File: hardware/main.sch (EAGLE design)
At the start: 16 parts, among them IC1 ATMEGA168-AU, J1 AVR_SPI_PRG_6NS

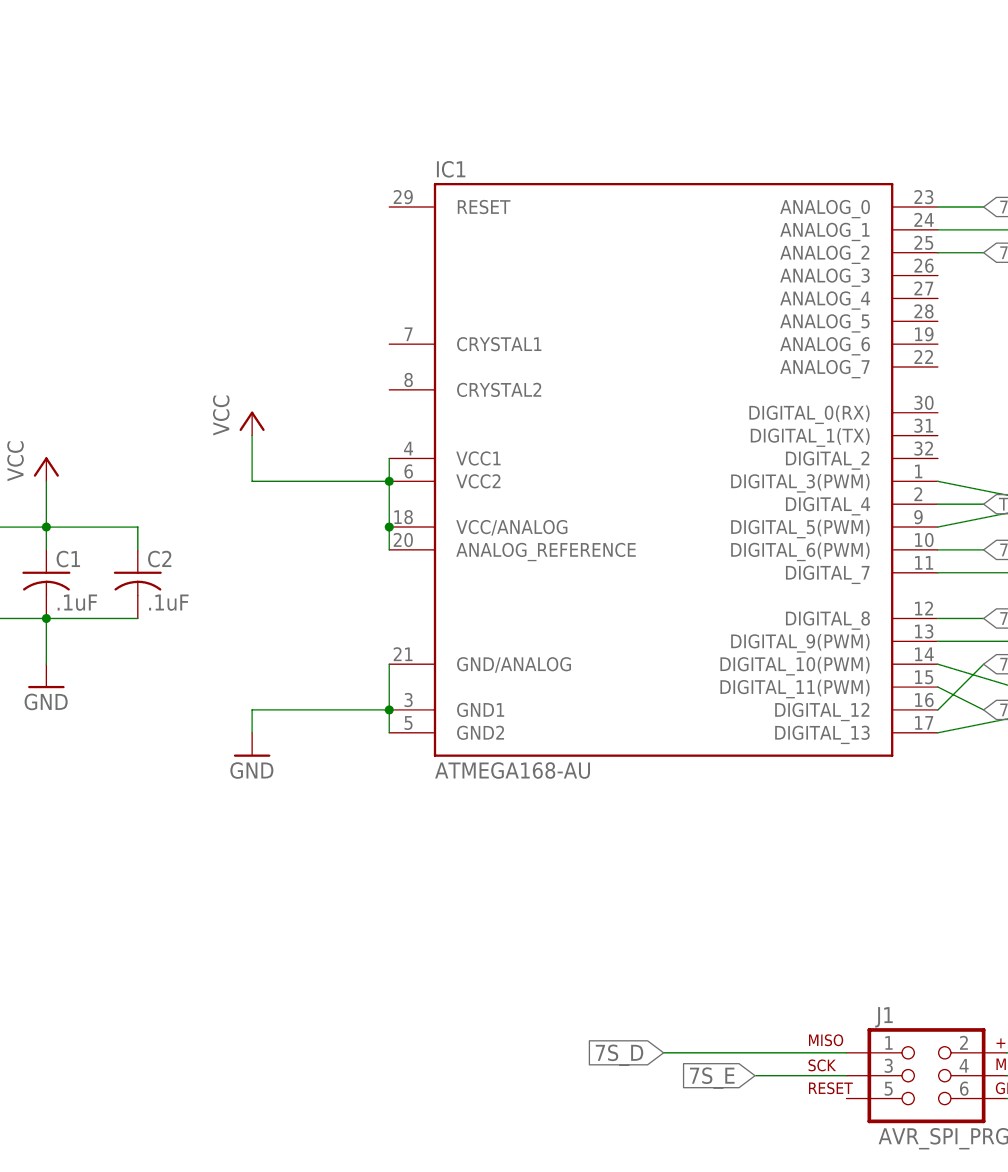
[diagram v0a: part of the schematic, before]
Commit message: HARDWARE MISTAKE: Did not include connection to Reset line. This makes the AVR unprogrammable without a jumper wire. Fixed.
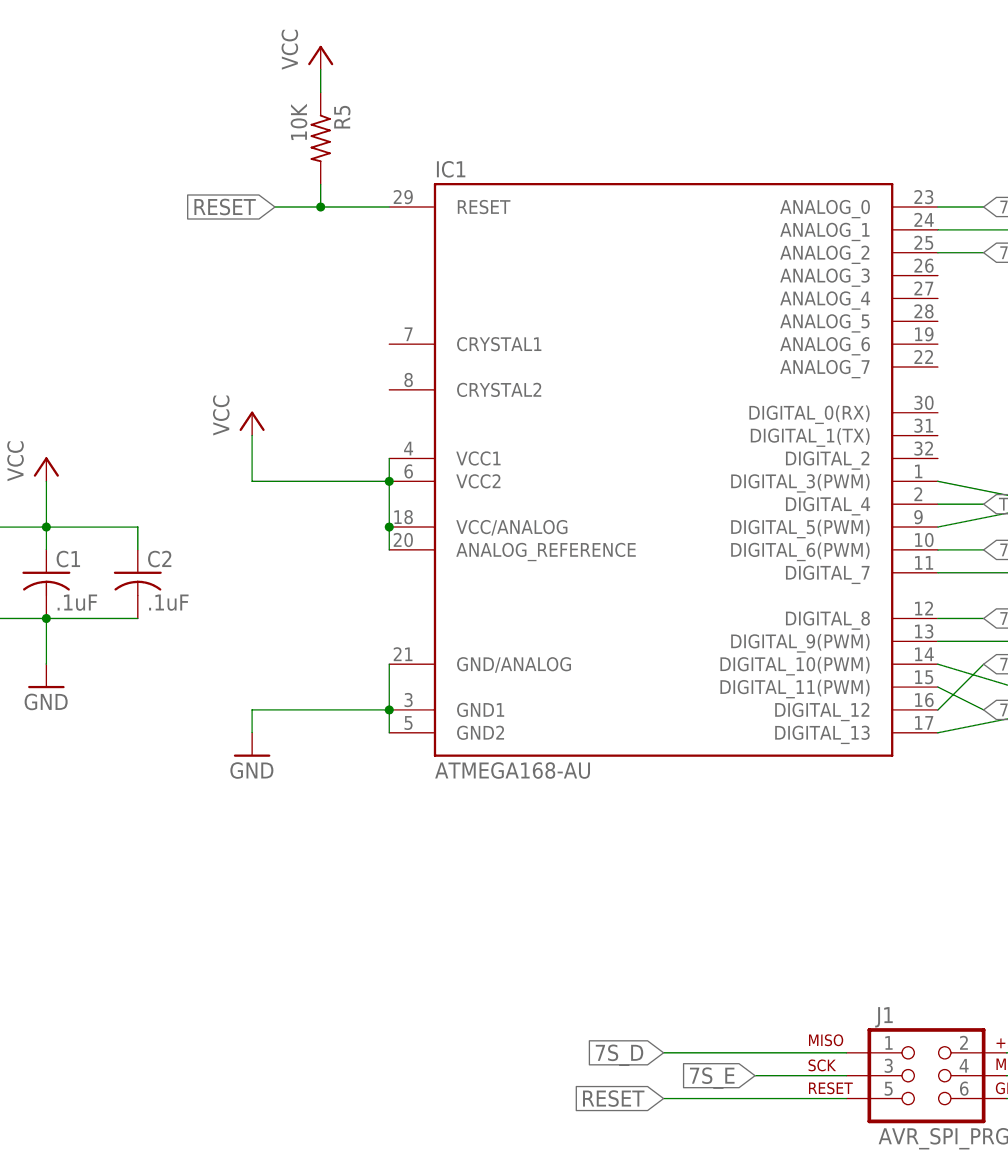
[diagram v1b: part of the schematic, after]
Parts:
- added R5: 10K, rcl:R-US_M0805
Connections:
- new net RESET: IC1.RESET, J1.5, R5.2
- net VCC: now also R5.1
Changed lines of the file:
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@@
 <part name="GND3" library="supply1" deviceset="GND" device=""/>
 <part name="P+3" library="supply1" deviceset="VCC" device=""/>
+<part name="P+4" library="supply1" deviceset="VCC" device=""/>
+<part name="R5" library="rcl" deviceset="R-US_" device="M0805" value="10K"/>
 </parts>
 <sheets>
@@
 <instance part="GND3" gate="1" x="121.92" y="132.08"/>
 <instance part="P+3" gate="VCC" x="114.3" y="144.78"/>
+<instance part="P+4" gate="VCC" x="33.02" y="251.46"/>
+<instance part="R5" gate="G$1" x="33.02" y="241.3" rot="R270"/>
 </instances>
 <busses>
@@
 <wire x1="114.3" y1="139.7" x2="114.3" y2="142.24" width="0.1524" layer="91"/>
 </segment>
+<segment>
+<pinref part="R5" gate="G$1" pin="1"/>
+<pinref part="P+4" gate="VCC" pin="VCC"/>
+<wire x1="33.02" y1="246.38" x2="33.02" y2="248.92" width="0.1524" layer="91"/>
+</segment>
 </net>
 <net name="GND" class="0">
@@
 </segment>
 </net>
+<net name="RESET" class="0">
+<segment>
+<pinref part="J1" gate="G$1" pin="5"/>
+<wire x1="91.44" y1="134.62" x2="71.12" y2="134.62" width="0.1524" layer="91"/>
+<label x="71.12" y="134.62" size="1.778" layer="95" rot="MR0" xref="yes"/>
+</segment>
+<segment>
+<pinref part="IC1" gate="1" pin="RESET"/>
+<wire x1="40.64" y1="233.68" x2="33.02" y2="233.68" width="0.1524" layer="91"/>
+<label x="27.94" y="233.68" size="1.778" layer="95" rot="MR0" xref="yes"/>
+<pinref part="R5" gate="G$1" pin="2"/>
+<wire x1="33.02" y1="233.68" x2="27.94" y2="233.68" width="0.1524" layer="91"/>
+<wire x1="33.02" y1="236.22" x2="33.02" y2="233.68" width="0.1524" layer="91"/>
+<junction x="33.02" y="233.68"/>
+</segment>
+</net>

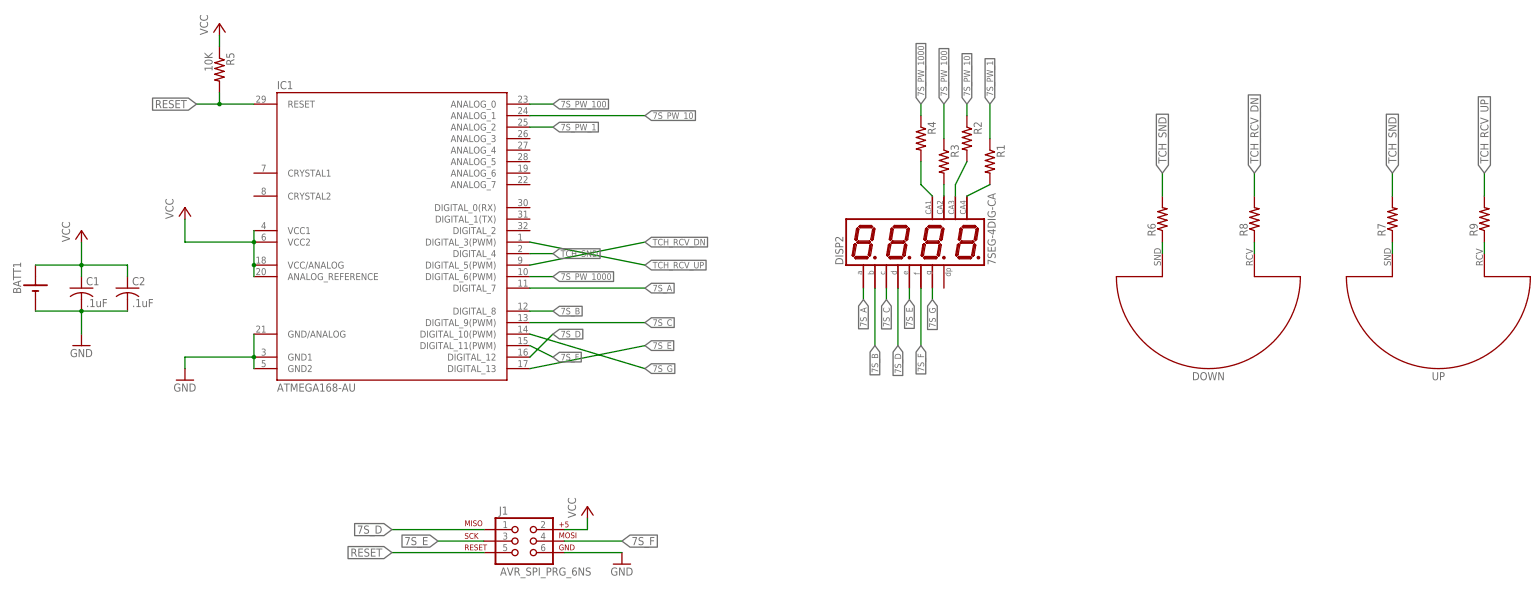
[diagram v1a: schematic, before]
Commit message: Hardware updates: 1. Changed display connection for cleaner layout 2. Changed touch sensor configuration for CVD touch sensing, and simpler layout 3. Changed passives to 0603 to ensmallen the board 4. Ensmallened the board 5. Rounded them corners
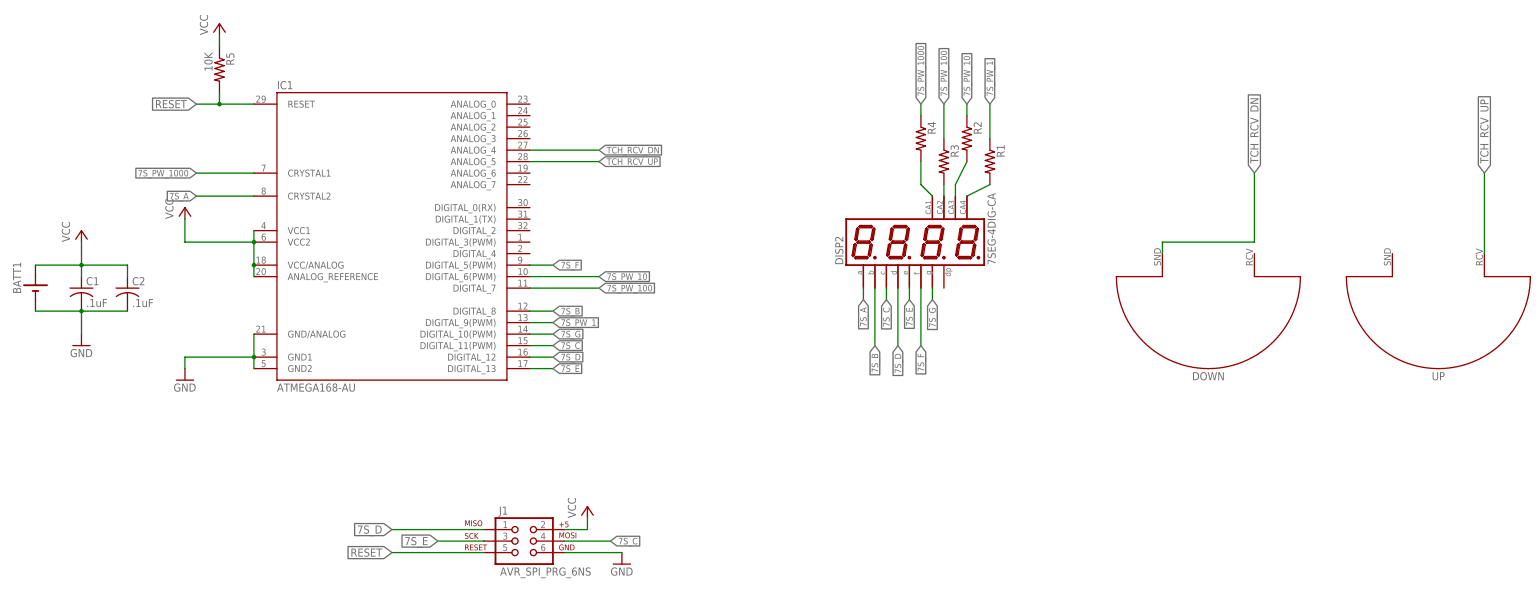
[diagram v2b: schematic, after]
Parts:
- removed R6, R7, R8, R9: (no value), rcl:R-US_M0805
- C1, C2: device rcl:C-USC0805 -> rcl:C-USC0603
- R1, R2, R3, R4, R5: device rcl:R-US_M0805 -> rcl:R-US_R0603
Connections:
- removed net N$1: DOWN.SND, R6.1
- removed net N$6: DOWN.RCV, R8.1
- removed net N$7: R7.1, UP.SND
- removed net N$8: R9.1, UP.RCV
- removed net TCH_SND: IC1.DIGITAL_4, R6.2, R7.2
- net 7S_A: now also IC1.CRYSTAL2; no longer IC1.DIGITAL_7
- net 7S_C: now also IC1.DIGITAL_11(PWM), J1.4; no longer IC1.DIGITAL_9(PWM)
- net 7S_F: now also IC1.DIGITAL_5(PWM); no longer IC1.DIGITAL_11(PWM), J1.4
- net 7S_PW_1: now also IC1.DIGITAL_9(PWM); no longer IC1.ANALOG_2
- net 7S_PW_10: now also IC1.DIGITAL_6(PWM); no longer IC1.ANALOG_1
- net 7S_PW_100: now also IC1.DIGITAL_7; no longer IC1.ANALOG_0
- net 7S_PW_1000: now also IC1.CRYSTAL1; no longer IC1.DIGITAL_6(PWM)
- net TCH_RCV_DN: now also DOWN.SND, IC1.ANALOG_4; no longer IC1.DIGITAL_5(PWM), R8.2
- net TCH_RCV_UP: now also IC1.ANALOG_5, UP.RCV; no longer IC1.DIGITAL_3(PWM), R9.2
